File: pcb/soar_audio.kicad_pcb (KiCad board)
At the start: 4 copper layers, 79 x 51 mm, 107 parts, among them J1 RJ45-FLAPS, J2 RJ12-FLAPS, J3 HEADER_4, J4 Screw_Terminal_01x02, J5 RJ45-CAN, J6 HEADER_4, J7 HEADER_2, J8 HEADER_4, J9 HEADER_4, Q1 AO3401A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

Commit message: replaced out of stock inductor
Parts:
- L1: footprint Inductor_SMD:L_Bourns-SRN4018 -> OWN_PARTS:MWSA0402S
- moved C7 0.51 mm to (133.3, 69.8)
- moved L1 0.31 mm to (134.8, 73.2), turned to 180 degrees
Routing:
- net GND: track 91.5 -> 99.1 mm
- net Net-(C7-Pad2): track 1.85 -> 2.37 mm
- net Net-(C7-Pad1): track 7.93 -> 8.43 mm

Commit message: some minor changes
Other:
- outline, holes or cut-outs redrawn
- board text added: "."
- board text added: ">= 4 Ohm"
- board text removed: "4 - 8 Ohm"
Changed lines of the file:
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@@
   )
   (paper "A4")
+  (title_block
+    (title "the SOAR Utility")
+    (date "2022-01-05")
+    (rev "v1.0")
+  )
   (layers
     (0 "F.Cu" signal)
@@
   (gr_line (start 103 118) (end 179 118) (layer "Edge.Cuts") (width 0.1))
   (gr_circle (center 178 114) (end 178.576 114) (layer "Edge.Cuts") (width 0.249) (fill none))
+  (gr_circle (center 173.99 91.44) (end 174.99 91.44) (layer "Edge.Cuts") (width 0.2) (fill none))
   (gr_arc (start 103 118) (mid 101.93934 117.56066) (end 101.5 116.5) (layer "Edge.Cuts") (width 0.1))
   (gr_circle (center 174.006 72.644) (end 175.006 72.644) (layer "Edge.Cuts") (width 0.2) (fill none))
@@
   (gr_circle (center 104 114) (end 104.576 114) (layer "Edge.Cuts") (width 0.249) (fill none))
   (gr_arc (start 180.5 116.5) (mid 180.06066 117.56066) (end 179 118) (layer "Edge.Cuts") (width 0.1))
+  (gr_circle (center 173.99 87.63) (end 174.99 87.63) (layer "Edge.Cuts") (width 0.2) (fill none))
   (gr_text "pcbDesign:" (at 128.27 115.316) (layer "B.SilkS")
     (effects (font (size 0.8 0.8) (thickness 0.1)) (justify mirror))
@@
     (effects (font (size 1 1) (thickness 0.15)))
   )
+  (gr_text "." (at 131.064 68.834) (layer "F.SilkS")
+    (effects (font (size 1.5 1.5) (thickness 0.3)))
+  )
   (gr_text "the" (at 120.396 77.216) (layer "F.SilkS")
     (effects (font (size 1.25 1.25) (thickness 0.2)))
@@
     (effects (font (size 1 1) (thickness 0.15)))
   )
-  (gr_text "4 - 8 Ohm" (at 167.386 78.994) (layer "F.SilkS")
+  (gr_text ">= 4 Ohm" (at 167.132 78.74) (layer "F.SilkS")
     (effects (font (size 1 1) (thickness 0.15)))
   )
@@
     (effects (font (size 1 1) (thickness 0.15)))
   )
+  (gr_text "." (at 157.988 70.866) (layer "F.SilkS")
+    (effects (font (size 1.5 1.5) (thickness 0.3)))
+  )
   (gr_text "I2C2" (at 178.562 86.106) (layer "F.SilkS")
     (effects (font (size 1 1) (thickness 0.15)))
@@
     (effects (font (size 1 1) (thickness 0.15)))
   )
+  (gr_text "." (at 119.634 96.774) (layer "F.SilkS")
+    (effects (font (size 1.5 1.5) (thickness 0.3)))
+  )
   (gr_text "5V" (at 137.16 76.962 90) (layer "F.SilkS")
     (effects (font (size 1 1) (thickness 0.15)))
@@
     (effects (font (size 0.8 0.8) (thickness 0.1)))
   )
+  (gr_text "." (at 112.014 94.488) (layer "F.SilkS")
+    (effects (font (size 1.5 1.5) (thickness 0.3)))
+  )
   (segment (start 110.744 71.12) (end 104.394 77.47) (width 0.5) (layer "F.Cu") (net 1))

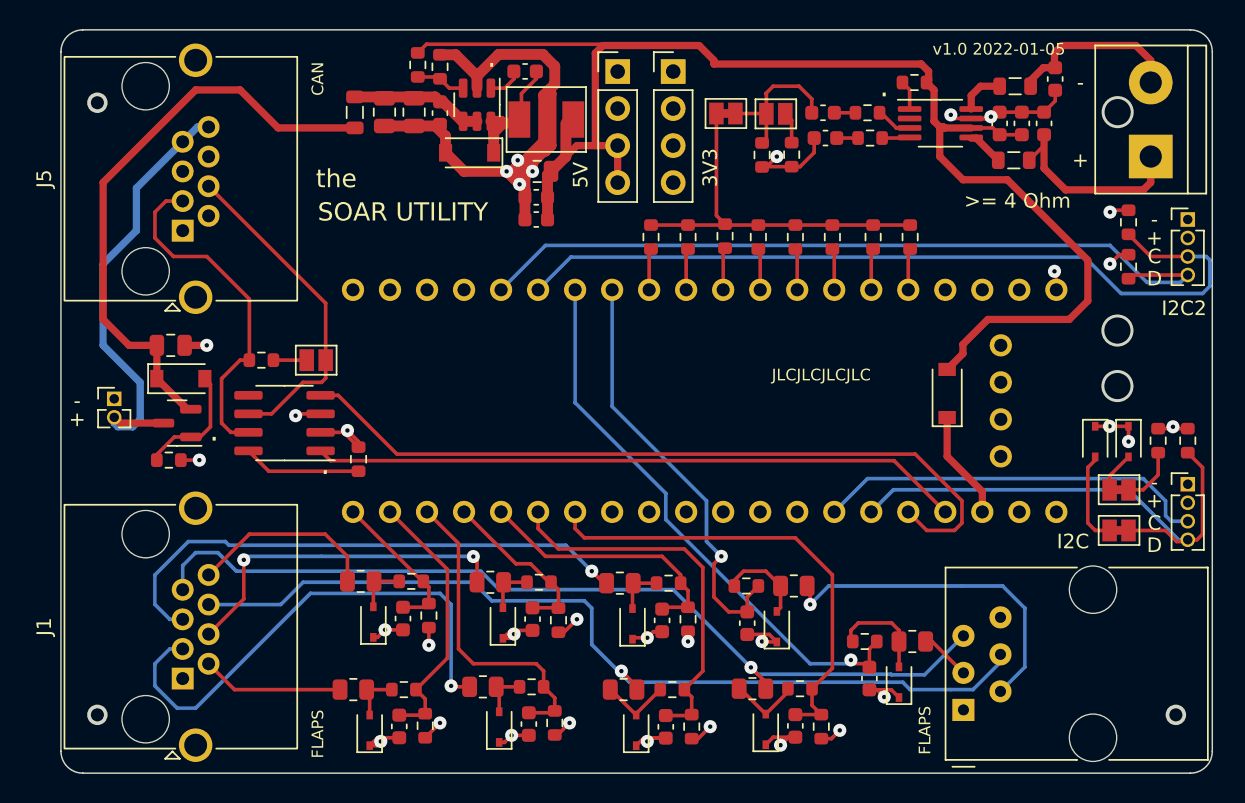
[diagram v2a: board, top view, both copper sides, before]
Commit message: updates based on feedback from Klaus
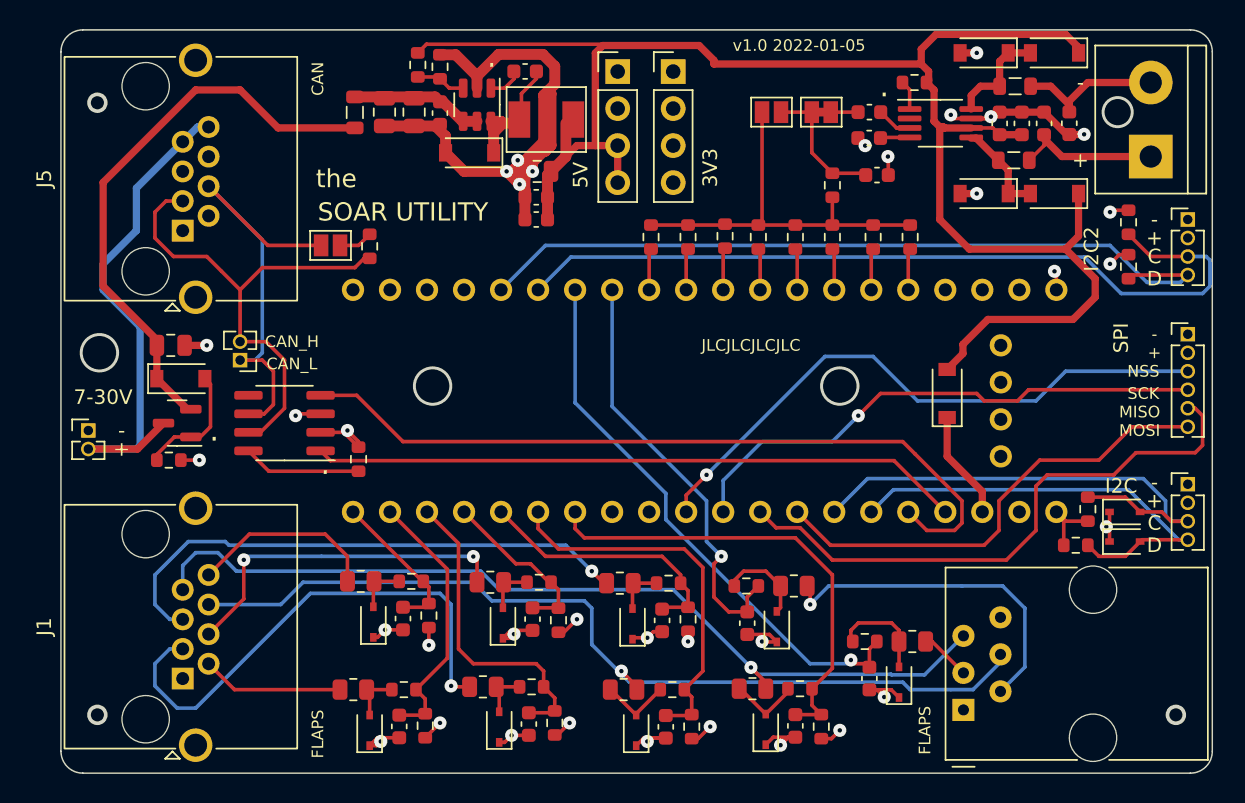
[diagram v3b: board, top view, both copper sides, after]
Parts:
- removed JP3, JP4: Jumper_Bridged, Jumper:SolderJumper-2_P1.3mm_Bridged_Pad1.0x1.5mm
- removed R11, R12: R100, Resistor_SMD:R_0603_1608Metric
- removed R47: 10k, Resistor_SMD:R_0603_1608Metric
- added C23: 2n7, Capacitor_SMD:C_0603_1608Metric, F.Cu at (157.5, 77.0)
- added D10: D_B5819W, Diode_SMD:D_SOD-123, F.Cu at (169.7, 78.2)
- added D11: D_B5819W, Diode_SMD:D_SOD-123, F.Cu at (164.8, 78.2)
- added D8: D_B5819W, Diode_SMD:D_SOD-123, F.Cu at (169.7, 68.6)
- added D9: D_B5819W, Diode_SMD:D_SOD-123, F.Cu at (164.8, 68.6)
- added J10: HEADER_2, Connector_PinHeader_1.27mm:PinHeader_1x02_P1.27mm_Vertical, F.Cu at (113.8, 89.7)
- added J11: HEADER_6, Connector_PinHeader_1.27mm:PinHeader_1x06_P1.27mm_Vertical, F.Cu at (178.8, 87.9)
- R9: value 10k -> 68k
- moved R14 10.8 mm to (122.7, 81.9), turned to 90 degrees
- moved R16 10.5 mm to (171.1, 102.4), turned to 0 degrees
- moved JP2 7.94 mm to (120.0, 81.8), turned to 0 degrees
- moved D6 7.15 mm to (174.5, 102.1), turned to 0 degrees
- moved R15 6.74 mm to (172.0, 99.9), turned to 90 degrees
- moved JP1 6.54 mm to (153.7, 72.6)
- moved R9 5.25 mm to (154.4, 77.7), turned to 90 degrees
- moved D5 4.83 mm to (174.5, 100.1), turned to 0 degrees
- moved C16 3.19 mm to (170.7, 73.4)
- moved C12 3.18 mm to (157.0, 72.6)
- moved C11 3.00 mm to (157.0, 74.4)
- moved J7 2.81 mm to (103.4, 94.5)
- moved JP5 0.32 mm to (150.3, 72.6), turned to 180 degrees
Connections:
- C12 pad 1: Net-(C12-Pad1) -> Net-(U4-Pad3)
- D5 pad 2: Net-(D5-Pad2) -> SCL
- D6 pad 2: Net-(D6-Pad2) -> SDA
- JP1 pad 1: AIN+ -> Net-(JP1-Pad1)
- JP5 pad 1: Net-(C12-Pad2) -> Net-(JP1-Pad1)
- JP5 pad 2: Net-(JP5-Pad2) -> AIN+
- R9 pad 1: Net-(C12-Pad2) -> AIN+
- R9 pad 2: GND -> Net-(JP1-Pad1)
- U4 pad 3: Net-(R11-Pad2) -> Net-(U4-Pad3)
- U4 pad 4: Net-(R12-Pad2) -> Net-(C11-Pad2)
- U6 pad PA15: unconnected-(U6-PadPA15) -> NSS
- U6 pad PB3: unconnected-(U6-PadPB3) -> SCK
- U6 pad PB4: unconnected-(U6-PadPB4) -> MISO
- U6 pad PB5: unconnected-(U6-PadPB5) -> MOSI
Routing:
- net NSS: track 0.00 -> 41.6 mm, vias 0 -> 1
- net MISO: track 0.00 -> 40.0 mm
- net SCK: track 0.00 -> 37.0 mm, vias 0 -> 1
- net MOSI: track 0.00 -> 32.3 mm
- net +5V: track 96.8 -> 116.6 mm
- net CAN_H: track 24.0 -> 34.7 mm
- net Net-(JP1-Pad1): track 0.00 -> 9.23 mm
- net Net-(C12-Pad2): track 10.3 -> 1.88 mm
- net CAN_L: track 22.8 -> 30.9 mm
- net Net-(D6-Pad2): track 6.45 -> 0.00 mm
- net VSUPPLY_IN: track 30.6 -> 35.9 mm
- net Net-(C15-Pad1): track 14.4 -> 10.3 mm
- net Net-(U4-Pad5): track 2.49 -> 6.58 mm
- net Net-(U4-Pad8): track 3.14 -> 7.20 mm
- net SDA: track 35.4 -> 31.4 mm
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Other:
- outline, holes or cut-outs redrawn
- board text added: "7-30V"
- board text added: "CAN_H"
- board text added: "CAN_L"
- board text added: "MISO"
- board text added: "MOSI"
- board text added: "NSS"
- board text added: "SCK"
- board text added: "SPI"
- board text removed: ">= 4 Ohm"

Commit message: finalized pcb and generated v1.0 production files
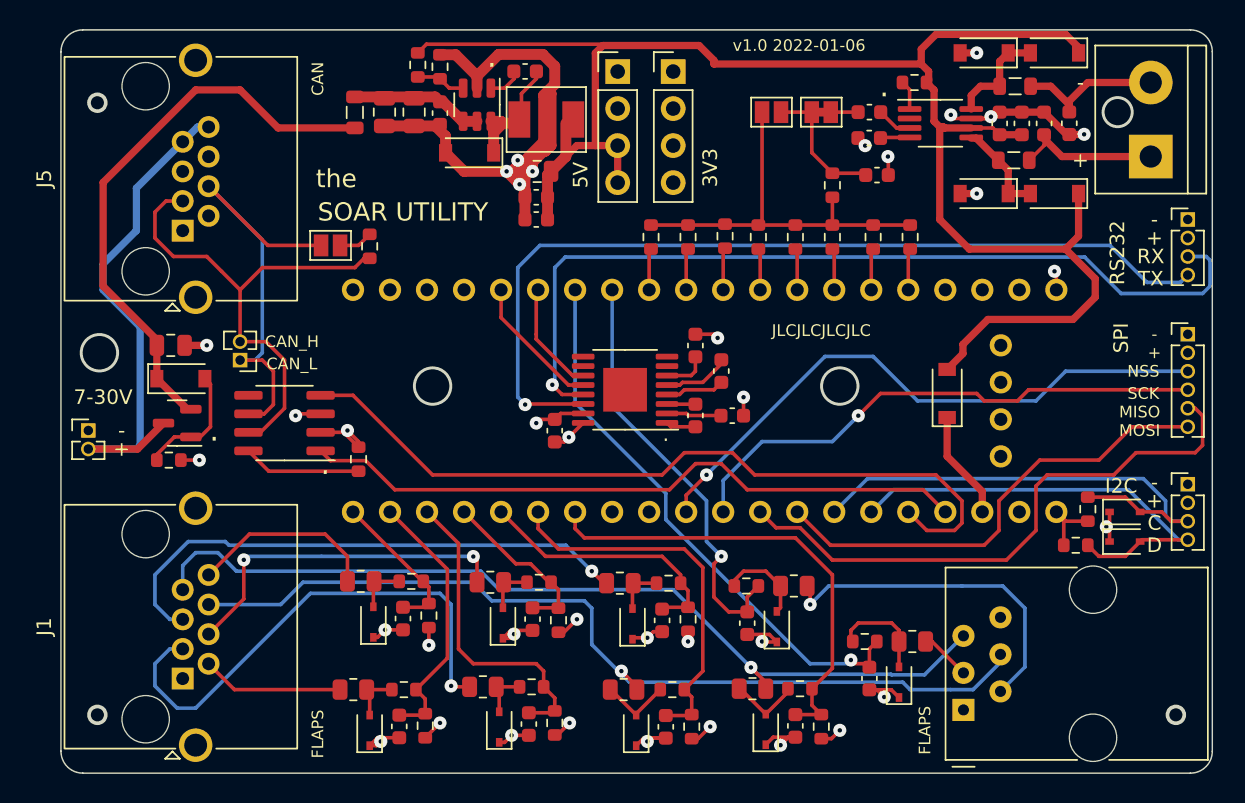
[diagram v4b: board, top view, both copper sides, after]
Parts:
- removed R43, R46: 4k7, Resistor_SMD:R_0603_1608Metric
- added C24: 100n, Capacitor_SMD:C_0603_1608Metric, F.Cu at (145.0, 93.5)
- added C25: 100n, Capacitor_SMD:C_0603_1608Metric, F.Cu at (135.4, 94.5)
- added C27: 100n, Capacitor_SMD:C_0603_1608Metric, F.Cu at (146.8, 90.4)
- added C28: 100n, Capacitor_SMD:C_0603_1608Metric, F.Cu at (147.6, 93.5)
- added C29: 100n, Capacitor_SMD:C_0603_1608Metric, F.Cu at (145.0, 88.7)
- added U2: MAX3232, Package_SO:HTSSOP-16-1EP_4.4x5mm_P0.65mm_EP3x3mm, F.Cu at (140.2, 91.7)
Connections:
- J3 pad 3: SCL2 -> RS232_RX
- J3 pad 4: SDA2 -> RS232_TX
- U6 pad PB10: SCL2 -> UART_TX
- U6 pad PB11: SDA2 -> UART_RX
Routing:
- net RS232_TX: track 0.00 -> 61.5 mm, vias 0 -> 1
- net RS232_RX: track 0.00 -> 60.4 mm, vias 0 -> 1
- net SCL2: track 56.4 -> 0.00 mm
- net SDA2: track 53.8 -> 0.00 mm
- net UART_RX: track 0.00 -> 9.46 mm
- net UART_TX: track 0.00 -> 7.69 mm
- net GND: track 97.6 -> 104.0 mm, vias 24 -> 27
- net Net-(C27-Pad1): track 0.00 -> 4.61 mm
- net Net-(C27-Pad2): track 0.00 -> 4.07 mm
- net Net-(C28-Pad2): track 0.00 -> 3.77 mm
- net Net-(C29-Pad2): track 0.00 -> 3.06 mm
- net Net-(C24-Pad2): track 0.00 -> 2.06 mm
- net Net-(C24-Pad1): track 0.00 -> 1.96 mm
- net CAN_TX: track 44.6 -> 46.1 mm
- net CAN_RX: track 52.9 -> 54.2 mm
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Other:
- board text added: "RS232"
- board text added: "RX"
- board text added: "TX"
- board text added: "v1.0 2022-01-06"
- board text removed: "I2C2"
- board text removed: "v1.0 2022-01-05"
